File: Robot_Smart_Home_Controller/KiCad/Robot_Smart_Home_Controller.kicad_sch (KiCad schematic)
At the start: 5 parts, among them SW1 SW_Push_SPDT, SW2 SW_Push_SPDT, SW3 SW_Push_SPDT, SW4 SW_Push_SPDT, SW5 SW_Push_SPDT

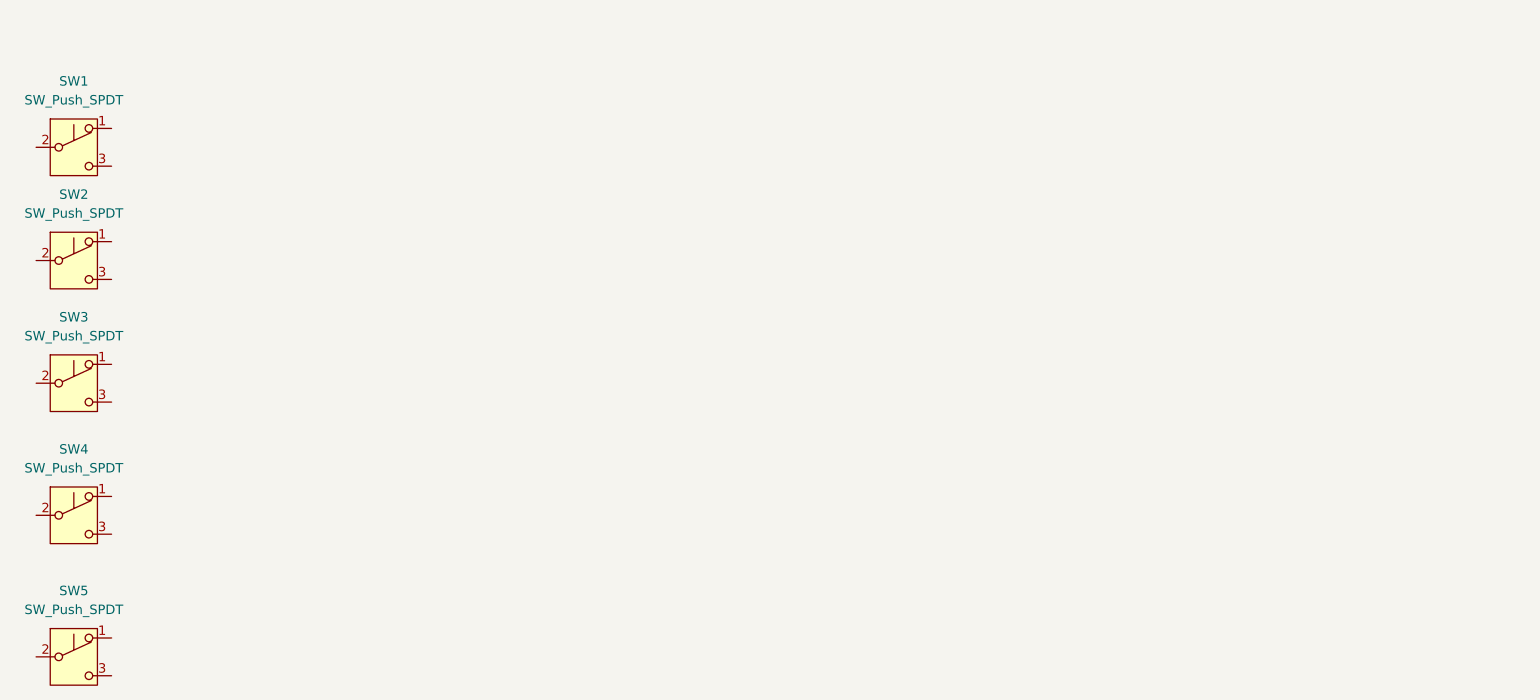
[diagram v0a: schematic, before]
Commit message: New schematic
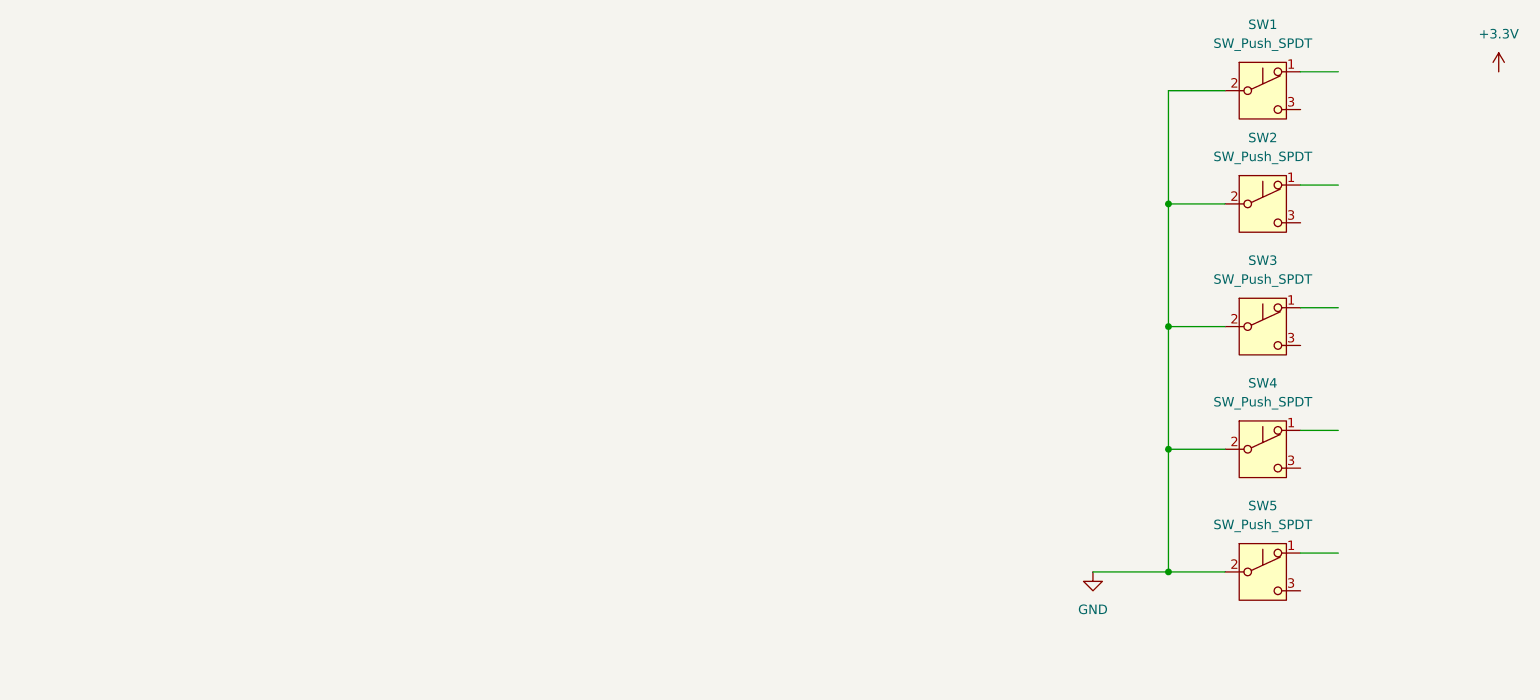
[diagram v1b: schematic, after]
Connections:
- net GND: now reaches SW5.2 (B)
- net GND: now also SW1.2 (B), SW2.2 (B), SW3.2 (B), SW4.2 (B)
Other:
- moved on the sheet: SW1, SW2, SW3, SW4, SW5
